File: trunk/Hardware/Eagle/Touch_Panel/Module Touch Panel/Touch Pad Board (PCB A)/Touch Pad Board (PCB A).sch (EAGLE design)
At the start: 50 parts, among them U1 SCT2024(CSOG,CSSG,CSTG,CSDG), U2 SCT2024(CSOG,CSSG,CSTG,CSDG), X0 TPTP10R, X1 TPTP10R, X2 TPTP10R, X3 TPTP10R, X4 TPTP10R, Y0 TPTP10R, Y1 TPTP10R, Y2 TPTP10R

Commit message: Work in progress
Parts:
- removed X0, X1, X2, X3, X4, Y0, Y1, Y2: TPTP10R, testpad:TPTP10R
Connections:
- removed net N$16: JP2.4, Y1.TP
- removed net N$41: JP2.3, Y0.TP
- removed net N$42: JP3.4, Y2.TP
- removed net N$44: JP4.4, X1.TP
- removed net N$45: JP4.3, X2.TP
- removed net N$46: JP4.2, X0.TP
- removed net N$48: JP5.2, X3.TP
- removed net N$51: JP5.4, X4.TP
- new net X0: JP4.2
- new net X1: JP4.4
- new net X2: JP4.3
- new net X3: JP5.2
- new net X4: JP5.4
- new net Y0: JP2.3
- new net Y1: JP2.4
- new net Y2: JP3.4

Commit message: Board of TPB (PCB A) - :)Done
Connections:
- net GND: now also JP2.3, JP2.4, JP3.2; no longer JP2.1, JP2.2, JP3.3
- net Y0: now also JP2.2; no longer JP2.3
- net Y1: now also JP2.1; no longer JP2.4
- net Y2: now also JP3.3; no longer JP3.4
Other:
- moved on the sheet: JP2

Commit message: Work in progress
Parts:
- added R5: 10, resistor:R-EU_R0805
- added U$1: PHOTO_TRANS, myHome:PHOTO_TRANS
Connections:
- new net N$15: JP3.1, R5.2, U$1.E
- net +3V3: now also U$1.C
- net GND: now also R5.1; no longer JP3.1
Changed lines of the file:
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@@
 <part name="GND7" library="supply1" deviceset="GND" device=""/>
 <part name="+3V4" library="supply1" deviceset="+3V3" device=""/>
+<part name="U$1" library="myHome" deviceset="PHOTO_TRANS" device=""/>
+<part name="R5" library="resistor" deviceset="R-EU_" device="R0805" value="10"/>
+<part name="+3V5" library="supply1" deviceset="+3V3" device=""/>
+<part name="GND8" library="supply1" deviceset="GND" device=""/>
 </parts>
 <sheets>
@@
 <instance part="GND7" gate="1" x="-10.16" y="48.26"/>
 <instance part="+3V4" gate="G$1" x="-10.16" y="73.66"/>
+<instance part="U$1" gate="G$1" x="-60.96" y="63.5"/>
+<instance part="R5" gate="G$1" x="-60.96" y="50.8" rot="R90"/>
+<instance part="+3V5" gate="G$1" x="-60.96" y="73.66"/>
+<instance part="GND8" gate="1" x="-60.96" y="40.64"/>
 </instances>
 <busses>
@@
 <segment>
 <pinref part="GND6" gate="1" pin="GND"/>
-<wire x1="-30.48" y1="53.34" x2="-30.48" y2="58.42" width="0.1524" layer="91"/>
-<pinref part="JP3" gate="A" pin="1"/>
-<wire x1="-35.56" y1="58.42" x2="-30.48" y2="58.42" width="0.1524" layer="91"/>
 <pinref part="JP3" gate="A" pin="2"/>
 <wire x1="-43.18" y1="58.42" x2="-43.18" y2="53.34" width="0.1524" layer="91"/>
 <wire x1="-43.18" y1="53.34" x2="-30.48" y2="53.34" width="0.1524" layer="91"/>
-<junction x="-30.48" y="53.34"/>
 </segment>
 <segment>
@@
 <junction x="-99.06" y="55.88"/>
 </segment>
+<segment>
+<pinref part="R5" gate="G$1" pin="1"/>
+<pinref part="GND8" gate="1" pin="GND"/>
+<wire x1="-60.96" y1="45.72" x2="-60.96" y2="43.18" width="0.1524" layer="91"/>
+</segment>
 </net>
 <net name="+3V3" class="0">
@@
 <pinref part="+3V4" gate="G$1" pin="+3V3"/>
 <wire x1="-10.16" y1="63.5" x2="-10.16" y2="71.12" width="0.1524" layer="91"/>
+</segment>
+<segment>
+<pinref part="+3V5" gate="G$1" pin="+3V3"/>
+<pinref part="U$1" gate="G$1" pin="C"/>
+<wire x1="-60.96" y1="71.12" x2="-60.96" y2="68.58" width="0.1524" layer="91"/>
 </segment>
 </net>
@@
 </segment>
 </net>
+<net name="N$15" class="0">
+<segment>
+<pinref part="U$1" gate="G$1" pin="E"/>
+<pinref part="R5" gate="G$1" pin="2"/>
+<wire x1="-60.96" y1="58.42" x2="-60.96" y2="55.88" width="0.1524" layer="91"/>
+<junction x="-60.96" y="55.88"/>
+<pinref part="JP3" gate="A" pin="1"/>
+<wire x1="-35.56" y1="58.42" x2="-33.02" y2="58.42" width="0.1524" layer="91"/>
+<wire x1="-33.02" y1="58.42" x2="-33.02" y2="55.88" width="0.1524" layer="91"/>
+<wire x1="-33.02" y1="55.88" x2="-60.96" y2="55.88" width="0.1524" layer="91"/>
+</segment>
+</net>

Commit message: Work in progress
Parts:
- R5: value 10 -> 4k6
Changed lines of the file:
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@@
 <part name="+3V4" library="supply1" deviceset="+3V3" device=""/>
 <part name="U$1" library="myHome" deviceset="PHOTO_TRANS" device=""/>
-<part name="R5" library="resistor" deviceset="R-EU_" device="R0805" value="10"/>
+<part name="R5" library="resistor" deviceset="R-EU_" device="R0805" value="4k6"/>
 <part name="+3V5" library="supply1" deviceset="+3V3" device=""/>
 <part name="GND8" library="supply1" deviceset="GND" device=""/>

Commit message: Touch Panel PCB_A & PCB_B final version (to electrical&part check)
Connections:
- net N$15 renamed OPTO
- removed net X3: JP5.2
- new net X5: JP5.4
- net N$34: no longer JP1.3
- net X4: now also JP5.2; no longer JP5.4
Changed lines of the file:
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@@
 <wire x1="17.78" y1="50.8" x2="17.78" y2="0" width="0.1524" layer="91"/>
 <wire x1="17.78" y1="0" x2="30.48" y2="0" width="0.1524" layer="91"/>
-<pinref part="JP1" gate="A" pin="3"/>
-<wire x1="-7.62" y1="55.88" x2="-7.62" y2="50.8" width="0.1524" layer="91"/>
-<wire x1="-7.62" y1="50.8" x2="17.78" y2="50.8" width="0.1524" layer="91"/>
-<junction x="17.78" y="50.8"/>
 </segment>
 </net>
@@
 </segment>
 </net>
-<net name="X3" class="0">
+<net name="X4" class="0">
 <segment>
 <pinref part="JP5" gate="A" pin="2"/>
@@
 </segment>
 </net>
-<net name="X4" class="0">
+<net name="X5" class="0">
 <segment>
 <pinref part="JP5" gate="A" pin="4"/>
@@
 </segment>
 </net>
-<net name="N$15" class="0">
+<net name="OPTO" class="0">
 <segment>
 <pinref part="U$1" gate="G$1" pin="E"/>

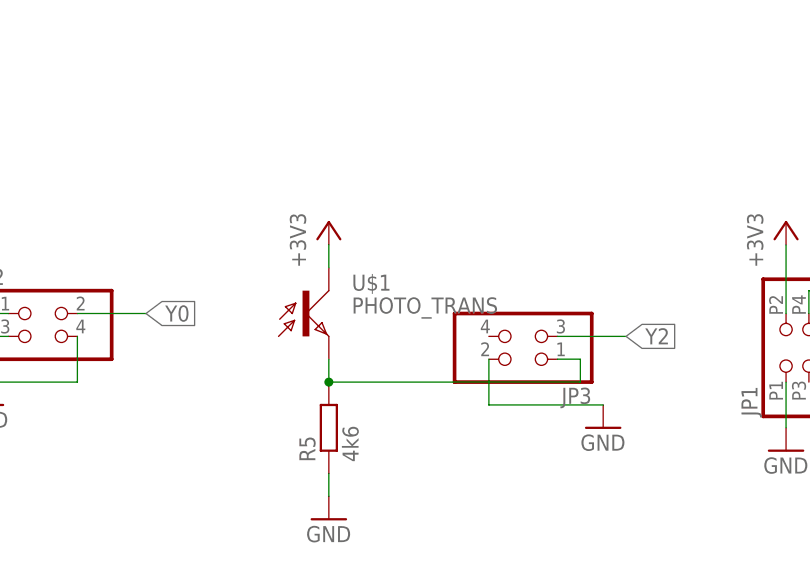
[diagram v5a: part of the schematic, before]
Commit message: Touch Panel (PCBA+PCBB) ver. 1.00
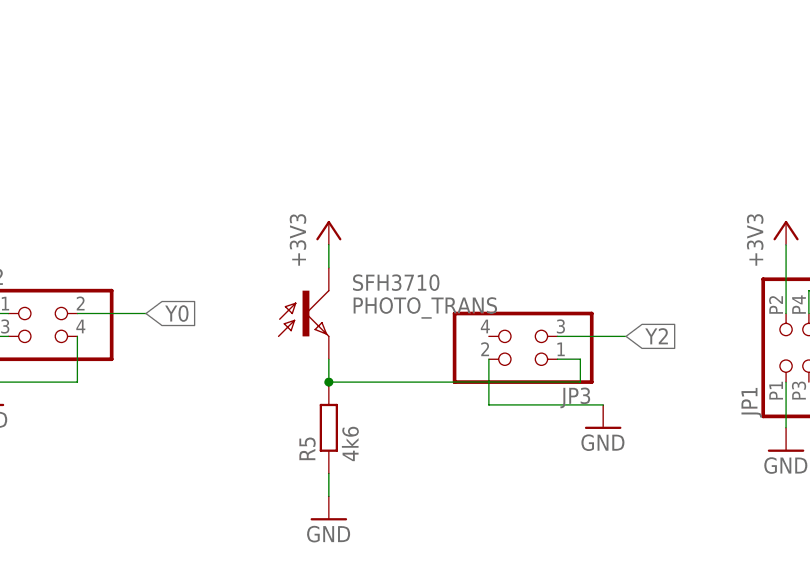
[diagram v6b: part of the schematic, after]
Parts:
- D1: device diode:DIODE-DO214AA -> diode:DIODE-DO214AC
- renumbered U$1 to SFH3710
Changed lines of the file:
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@@
 <grid distance="0.1" unitdist="inch" unit="inch" style="lines" multiple="1" display="no" altdistance="0.01" altunitdist="inch" altunit="inch"/>
 <layers>
-<layer number="1" name="Top" color="4" fill="1" visible="no" active="no"/>
-<layer number="2" name="Route2" color="1" fill="3" visible="no" active="no"/>
-<layer number="3" name="Route3" color="4" fill="3" visible="no" active="no"/>
-<layer number="4" name="Route4" color="1" fill="4" visible="no" active="no"/>
-<layer number="5" name="Route5" color="4" fill="4" visible="no" active="no"/>
-<layer number="6" name="Route6" color="1" fill="8" visible="no" active="no"/>
-<layer number="7" name="Route7" color="4" fill="8" visible="no" active="no"/>
-<layer number="8" name="Route8" color="1" fill="2" visible="no" active="no"/>
-<layer number="9" name="Route9" color="4" fill="2" visible="no" active="no"/>
-<layer number="10" name="Route10" color="1" fill="7" visible="no" active="no"/>
-<layer number="11" name="Route11" color="4" fill="7" visible="no" active="no"/>
-<layer number="12" name="Route12" color="1" fill="5" visible="no" active="no"/>
-<layer number="13" name="Route13" color="4" fill="5" visible="no" active="no"/>
-<layer number="14" name="Route14" color="1" fill="6" visible="no" active="no"/>
-<layer number="15" name="Route15" color="4" fill="6" visible="no" active="no"/>
-<layer number="16" name="Bottom" color="1" fill="1" visible="no" active="no"/>
-<layer number="17" name="Pads" color="2" fill="1" visible="no" active="no"/>
-<layer number="18" name="Vias" color="2" fill="1" visible="no" active="no"/>
-<layer number="19" name="Unrouted" color="6" fill="1" visible="no" active="no"/>
-<layer number="20" name="Dimension" color="15" fill="1" visible="no" active="no"/>
-<layer number="21" name="tPlace" color="7" fill="1" visible="no" active="no"/>
-<layer number="22" name="bPlace" color="7" fill="1" visible="no" active="no"/>
-<layer number="23" name="tOrigins" color="15" fill="1" visible="no" active="no"/>
-<layer number="24" name="bOrigins" color="15" fill="1" visible="no" active="no"/>
-<layer number="25" name="tNames" color="7" fill="1" visible="no" active="no"/>
-<layer number="26" name="bNames" color="7" fill="1" visible="no" active="no"/>
-<layer number="27" name="tValues" color="7" fill="1" visible="no" active="no"/>
-<layer number="28" name="bValues" color="7" fill="1" visible="no" active="no"/>
+<layer number="1" name="Top" color="4" fill="1" visible="yes" active="no"/>
+<layer number="2" name="Route2" color="1" fill="3" visible="yes" active="no"/>
+<layer number="3" name="Route3" color="4" fill="3" visible="yes" active="no"/>
+<layer number="4" name="Route4" color="1" fill="4" visible="yes" active="no"/>
+<layer number="5" name="Route5" color="4" fill="4" visible="yes" active="no"/>
+<layer number="6" name="Route6" color="1" fill="8" visible="yes" active="no"/>
+<layer number="7" name="Route7" color="4" fill="8" visible="yes" active="no"/>
+<layer number="8" name="Route8" color="1" fill="2" visible="yes" active="no"/>
+<layer number="9" name="Route9" color="4" fill="2" visible="yes" active="no"/>
+<layer number="10" name="Route10" color="1" fill="7" visible="yes" active="no"/>
+<layer number="11" name="Route11" color="4" fill="7" visible="yes" active="no"/>
+<layer number="12" name="Route12" color="1" fill="5" visible="yes" active="no"/>
+<layer number="13" name="Route13" color="4" fill="5" visible="yes" active="no"/>
+<layer number="14" name="Route14" color="1" fill="6" visible="yes" active="no"/>
+<layer number="15" name="Route15" color="4" fill="6" visible="yes" active="no"/>
+<layer number="16" name="Bottom" color="1" fill="1" visible="yes" active="no"/>
+<layer number="17" name="Pads" color="2" fill="1" visible="yes" active="no"/>
+<layer number="18" name="Vias" color="2" fill="1" visible="yes" active="no"/>
+<layer number="19" name="Unrouted" color="6" fill="1" visible="yes" active="no"/>
+<layer number="20" name="Dimension" color="15" fill="1" visible="yes" active="no"/>
+<layer number="21" name="tPlace" color="7" fill="1" visible="yes" active="no"/>
+<layer number="22" name="bPlace" color="7" fill="1" visible="yes" active="no"/>
+<layer number="23" name="tOrigins" color="15" fill="1" visible="yes" active="no"/>
+<layer number="24" name="bOrigins" color="15" fill="1" visible="yes" active="no"/>
+<layer number="25" name="tNames" color="7" fill="1" visible="yes" active="no"/>
+<layer number="26" name="bNames" color="7" fill="1" visible="yes" active="no"/>
+<layer number="27" name="tValues" color="7" fill="1" visible="yes" active="no"/>
+<layer number="28" name="bValues" color="7" fill="1" visible="yes" active="no"/>
 <layer number="29" name="tStop" color="7" fill="3" visible="no" active="no"/>
 <layer number="30" name="bStop" color="7" fill="6" visible="no" active="no"/>
@@
 <layer number="35" name="tGlue" color="7" fill="4" visible="no" active="no"/>
 <layer number="36" name="bGlue" color="7" fill="5" visible="no" active="no"/>
-<layer number="37" name="tTest" color="7" fill="1" visible="no" active="no"/>
-<layer number="38" name="bTest" color="7" fill="1" visible="no" active="no"/>
+<layer number="37" name="tTest" color="7" fill="1" visible="yes" active="no"/>
+<layer number="38" name="bTest" color="7" fill="1" visible="yes" active="no"/>
 <layer number="39" name="tKeepout" color="4" fill="11" visible="no" active="no"/>
 <layer number="40" name="bKeepout" color="1" fill="11" visible="no" active="no"/>
@@
 <layer number="44" name="Drills" color="7" fill="1" visible="no" active="no"/>
 <layer number="45" name="Holes" color="7" fill="1" visible="no" active="no"/>
-<layer number="46" name="Milling" color="3" fill="1" visible="no" active="no"/>
-<layer number="47" name="Measures" color="7" fill="1" visible="no" active="no"/>
-<layer number="48" name="Document" color="7" fill="1" visible="no" active="no"/>
-<layer number="49" name="Reference" color="7" fill="1" visible="no" active="no"/>
-<layer number="50" name="dxf" color="7" fill="1" visible="no" active="no"/>
-<layer number="51" name="tDocu" color="7" fill="1" visible="no" active="no"/>
-<layer number="52" name="bDocu" color="7" fill="1" visible="no" active="no"/>
+<layer number="46" name="Milling" color="3" fill="1" visible="yes" active="no"/>
+<layer number="47" name="Measures" color="7" fill="1" visible="yes" active="no"/>
+<layer number="48" name="Document" color="7" fill="1" visible="yes" active="no"/>
+<layer number="49" name="Reference" color="7" fill="1" visible="yes" active="no"/>
+<layer number="50" name="dxf" color="7" fill="1" visible="yes" active="no"/>
+<layer number="51" name="tDocu" color="7" fill="1" visible="yes" active="no"/>
+<layer number="52" name="bDocu" color="7" fill="1" visible="yes" active="no"/>
 <layer number="91" name="Nets" color="2" fill="1" visible="yes" active="yes"/>
 <layer number="92" name="Busses" color="1" fill="1" visible="yes" active="yes"/>
@@
 <part name="LED27" library="led" deviceset="LED" device="CHIPLED_1206" value="red"/>
 <part name="LED28" library="led" deviceset="LED" device="CHIPLED_1206" value="red"/>
-<part name="D1" library="diode" deviceset="DIODE-" device="DO214AA"/>
+<part name="D1" library="diode" deviceset="DIODE-" device="DO214AC"/>
 <part name="GND1" library="supply1" deviceset="GND" device=""/>
 <part name="+3V2" library="supply1" deviceset="+3V3" device=""/>
@@
 <part name="GND7" library="supply1" deviceset="GND" device=""/>
 <part name="+3V4" library="supply1" deviceset="+3V3" device=""/>
-<part name="U$1" library="myHome" deviceset="PHOTO_TRANS" device=""/>
+<part name="SFH3710" library="myHome" deviceset="PHOTO_TRANS" device=""/>
 <part name="R5" library="resistor" deviceset="R-EU_" device="R0805" value="4k6"/>
 <part name="+3V5" library="supply1" deviceset="+3V3" device=""/>
@@
 <instance part="GND7" gate="1" x="-10.16" y="48.26"/>
 <instance part="+3V4" gate="G$1" x="-10.16" y="73.66"/>
-<instance part="U$1" gate="G$1" x="-60.96" y="63.5"/>
+<instance part="SFH3710" gate="G$1" x="-60.96" y="63.5"/>
 <instance part="R5" gate="G$1" x="-60.96" y="50.8" rot="R90"/>
 <instance part="+3V5" gate="G$1" x="-60.96" y="73.66"/>
@@
 <segment>
 <pinref part="+3V5" gate="G$1" pin="+3V3"/>
-<pinref part="U$1" gate="G$1" pin="C"/>
+<pinref part="SFH3710" gate="G$1" pin="C"/>
 <wire x1="-60.96" y1="71.12" x2="-60.96" y2="68.58" width="0.1524" layer="91"/>
 </segment>
@@
 <net name="OPTO" class="0">
 <segment>
-<pinref part="U$1" gate="G$1" pin="E"/>
+<pinref part="SFH3710" gate="G$1" pin="E"/>
 <pinref part="R5" gate="G$1" pin="2"/>
 <wire x1="-60.96" y1="58.42" x2="-60.96" y2="55.88" width="0.1524" layer="91"/>
